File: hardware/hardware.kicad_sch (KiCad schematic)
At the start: 10 parts

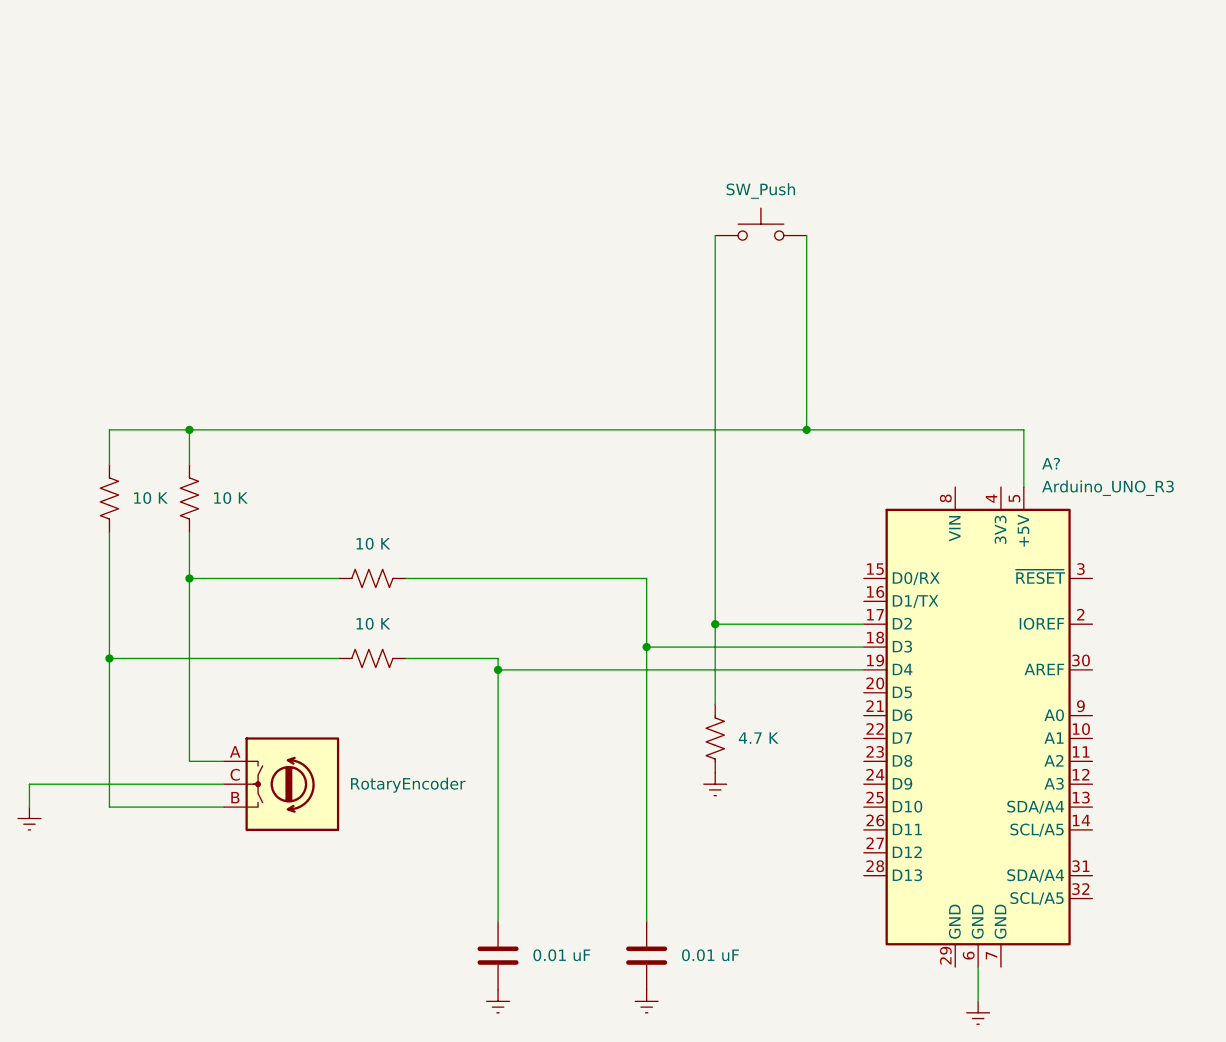
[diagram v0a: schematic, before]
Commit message: Added an LCD so that it can be used without a serial monitor
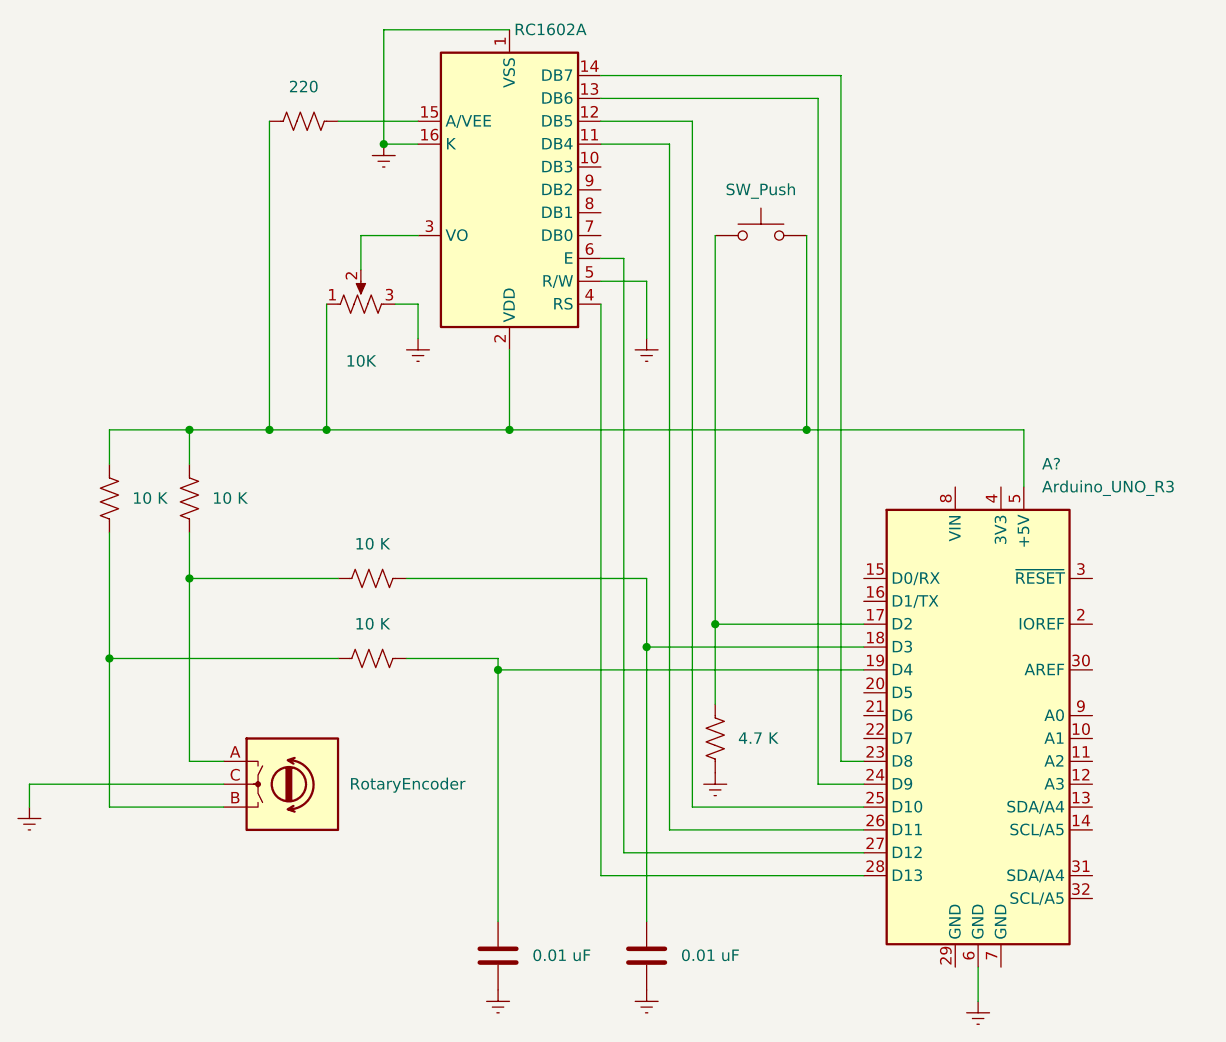
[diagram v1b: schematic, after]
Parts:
- added R?: 220, symbol Device:R_US
- added RV?: 10K, symbol Device:R_Potentiometer_US
- added U?: RC1602A, Display:RC1602A, symbol Display_Character:RC1602A
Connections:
- net Earth: now also C?.1, RV?.3, U?.1 (VSS), U?.16 (K), U?.5 (R/W); no longer C?.2
- net at A?.5 (+5V), R?.1, R?.1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: now also R?.1, RV?.1, U?.2 (VDD)
- net at A?.19 (D4), R?.2: now also C?.2; no longer C?.1
- net at A?.23 (D8): now also U?.14 (DB7)
- net at A?.24 (D9): now also U?.13 (DB6)
- net at A?.25 (D10): now also U?.12 (DB5)
- net at A?.26 (D11): now also U?.11 (DB4)
- net at A?.27 (D12): now also U?.6 (E)
- net at A?.28 (D13): now also U?.4 (RS)
- new net: RV?.2, U?.3 (VO)
- new net: R?.2, U?.15 (A/VEE)
